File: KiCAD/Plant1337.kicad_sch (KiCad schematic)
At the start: 47 parts, among them Q1 AO3400A, Q2 AO3400A, Q3 AO3400A, Q4 AO3400A, U1 SHTC3

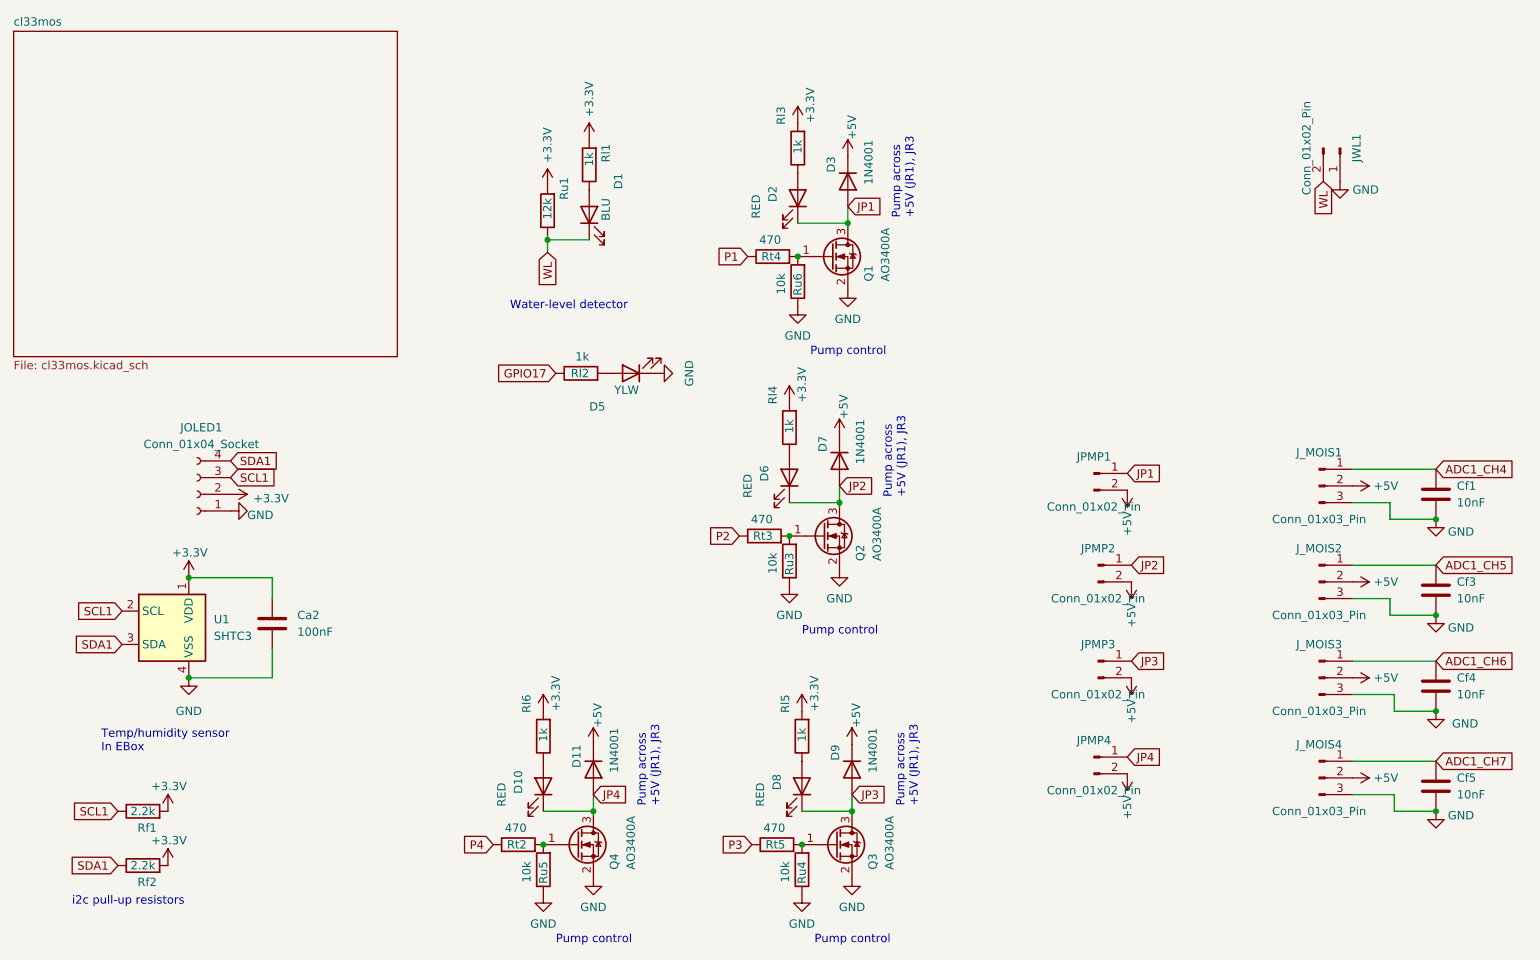
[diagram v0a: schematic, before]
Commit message: Add svelte-based web interface (#31)
- Add svelte-based web UI developed with the help of claude.
- KiCAD update -> v1.3.  Change pump2 DIO, remove pump pull-downs
- board v1.3, test web page

The old interface can still be reached by at the "/root" path.
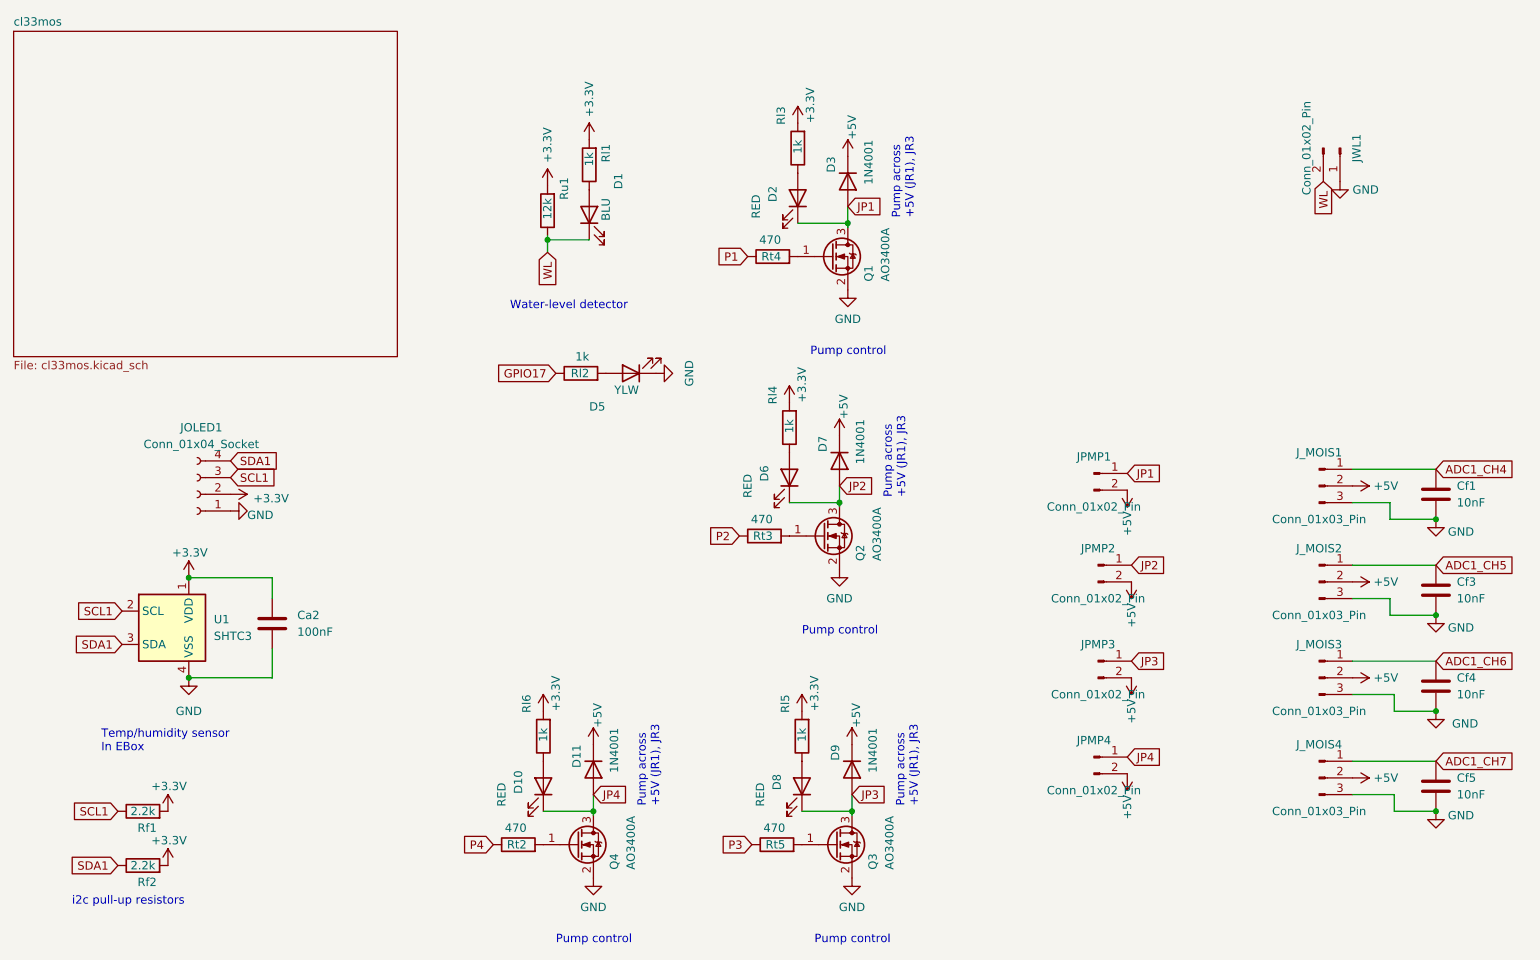
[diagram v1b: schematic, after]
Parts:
- removed Ru3, Ru4, Ru5, Ru6: 10k, Resistor_SMD:R_0603_1608Metric, symbol Device:R
